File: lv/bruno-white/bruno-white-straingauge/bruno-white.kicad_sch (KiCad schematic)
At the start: 5 parts, among them U1 HMC799LP3E

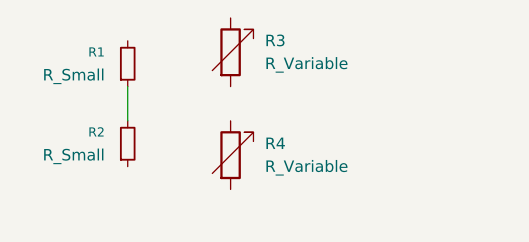
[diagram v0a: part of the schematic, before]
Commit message: LV and PE
I adjusted the wheatstone bridge circuit in my schematic, but I still have lots to do for that. Then for my PE buck converter I asked Edmund for some help and then I used the datasheet of the Buck DC DC converter to realize that it has a power transistor. So I added some components to that converter, but now I don't know what to do with the feedback.
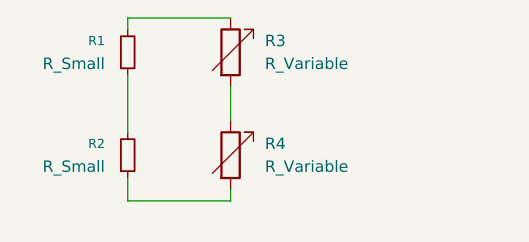
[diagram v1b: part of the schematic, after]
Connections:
- net at R4.1: now also R3.2
- net at R4.2: now also R2.1
- net at R1.2: now also R3.1
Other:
- moved on the sheet: R1, R2
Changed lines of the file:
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@@
 	(wire
 		(pts
-			(xy 107.95 46.99) (xy 107.95 50.8)
+			(xy 119.38 59.69) (xy 119.38 58.42)
+		)
+		(stroke
+			(width 0)
+			(type default)
+		)
+	)
+	(wire
+		(pts
+			(xy 107.95 39.37) (xy 119.38 39.37)
+		)
+		(stroke
+			(width 0)
+			(type default)
+		)
+	)
+	(wire
+		(pts
+			(xy 107.95 40.64) (xy 107.95 39.37)
+		)
+		(stroke
+			(width 0)
+			(type default)
+		)
+	)
+	(wire
+		(pts
+			(xy 107.95 45.72) (xy 107.95 52.07)
+		)
+		(stroke
+			(width 0)
+			(type default)
+		)
+	)
+	(wire
+		(pts
+			(xy 119.38 46.99) (xy 119.38 50.8)
+		)
+		(stroke
+			(width 0)
+			(type default)
+		)
+	)
+	(wire
+		(pts
+			(xy 107.95 59.69) (xy 107.95 57.15)
+		)
+		(stroke
+			(width 0)
+			(type default)
+		)
+	)
+	(wire
+		(pts
+			(xy 119.38 59.69) (xy 107.95 59.69)
 		)
 		(stroke
@@
 	(symbol
 		(lib_id "Device:R_Small")
-		(at 107.95 44.45 0)
+		(at 107.95 43.18 0)
 		(mirror x)
 		(unit 1)
@@
 		(dnp no)
 		(property "Reference" "R1"
-			(at 105.41 43.1799 0)
+			(at 105.41 41.9099 0)
 			(show_name no)
 			(do_not_autoplace no)
@@
 		)
 		(property "Value" "R_Small"
-			(at 105.41 45.7199 0)
+			(at 105.41 44.4499 0)
 			(show_name no)
 			(do_not_autoplace no)
@@
 		)
 		(property "Footprint" ""
-			(at 107.95 44.45 0)
+			(at 107.95 43.18 0)
 			(hide yes)
 			(show_name no)
@@
 		)
 		(property "Datasheet" ""
-			(at 107.95 44.45 0)
+			(at 107.95 43.18 0)
 			(hide yes)
 			(show_name no)
@@
 		)
 		(property "Description" "Resistor, small symbol"
-			(at 107.95 44.45 0)
+			(at 107.95 43.18 0)
 			(hide yes)
 			(show_name no)
@@
 	(symbol
 		(lib_id "Device:R_Small")
-		(at 107.95 53.34 0)
+		(at 107.95 54.61 0)
 		(mirror x)
 		(unit 1)
@@
 		(dnp no)
 		(property "Reference" "R2"
-			(at 105.41 52.0699 0)
+			(at 105.41 53.3399 0)
 			(show_name no)
 			(do_not_autoplace no)
@@
 		)
 		(property "Value" "R_Small"
-			(at 105.41 54.6099 0)
+			(at 105.41 55.8799 0)
 			(show_name no)
 			(do_not_autoplace no)
@@
 		)
 		(property "Footprint" ""
-			(at 107.95 53.34 0)
+			(at 107.95 54.61 0)
 			(hide yes)
 			(show_name no)
@@
 		)
 		(property "Datasheet" ""
-			(at 107.95 53.34 0)
+			(at 107.95 54.61 0)
 			(hide yes)
 			(show_name no)
@@
 		)
 		(property "Description" "Resistor, small symbol"
-			(at 107.95 53.34 0)
-			(hide yes)
-			(show_name no)
+			(at 107.95 54.61 0)
+			(hide yes)
+			(show_name no)

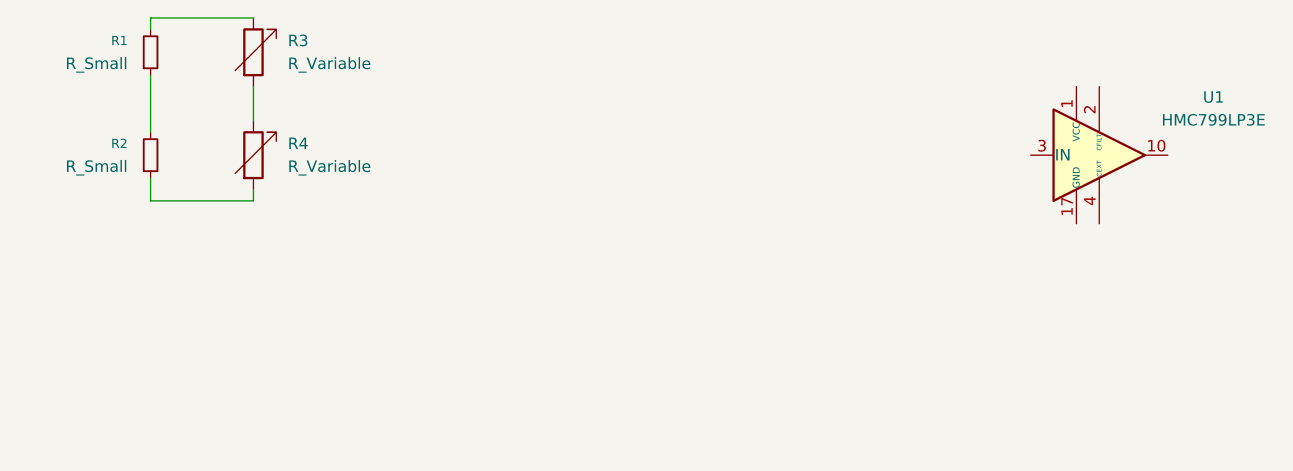
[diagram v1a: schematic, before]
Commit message: LV Strain Gauge Changes
I changed the wheatstone bridge circuit, but I'm still not sure if it's correct. I researched about the amplifier aspect of it and wrote some notes down. I figured out that we should use instrumentation amplifier (INA). I added that and did some schematics for INA, but I don't know what to do with V+ and V-.
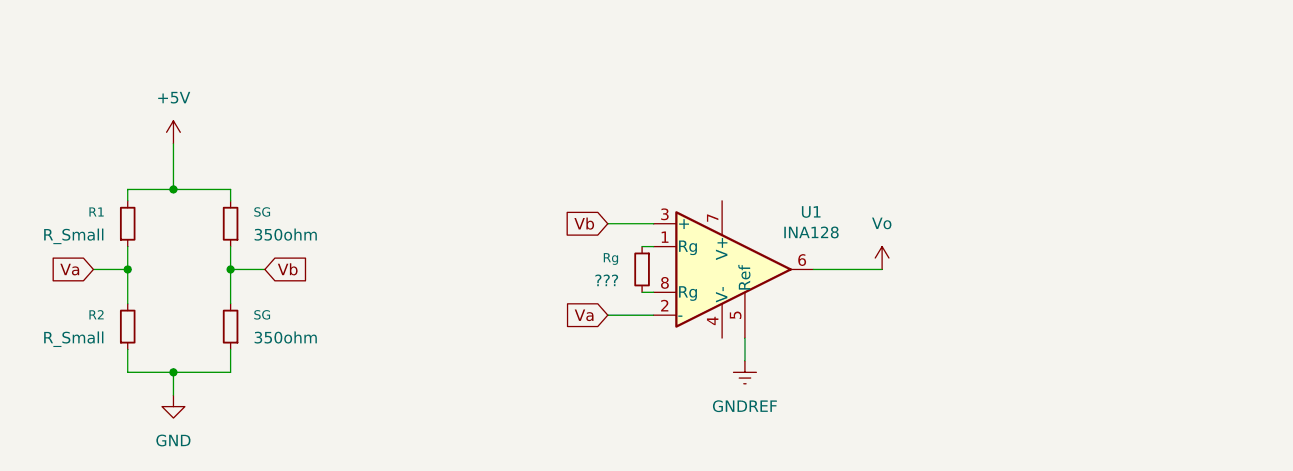
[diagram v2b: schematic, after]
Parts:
- removed R3, R4: R_Variable, Package_DFN_QFN:QFN-16-1EP_3x3mm_P0.5mm_EP1.75x1.75mm, symbol Device:R_Variable
- removed U1: HMC799LP3E, Package_DFN_QFN:QFN-16-1EP_3x3mm_P0.5mm_EP1.75x1.75mm, symbol Amplifier_Operational:HMC799LP3E
- added Rg: ???, symbol Device:R_Small
- added SG (x2): 350ohm, symbol Device:R_Small
- added U1: INA128, Package_SO:VSSOP-8_3x3mm_P0.65mm, symbol Amplifier_Instrumentation:INA128
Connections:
- net GND: now reaches R2.1
- net GND: now also SG.1
- net Va: now reaches R1.1, R2.2
- net Va: now also U1.2 (-)
- net +5V: now reaches R1.2
- net +5V: now also SG.2
- new net: Rg.1, U1.1 (Rg)
- new net: Rg.2, U1.8 (Rg)
- new net GNDREF: U1.5 (Ref)
- new net Vb: SG.1, SG.2, U1.3 (+)
- new net Vo: U1.6
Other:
- moved on the sheet: R1, R2
